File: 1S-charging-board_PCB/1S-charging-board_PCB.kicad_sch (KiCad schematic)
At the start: 4 parts, among them J1 Power Input, J2 Balance input, SW1 SW_Rotary_1x6_MP

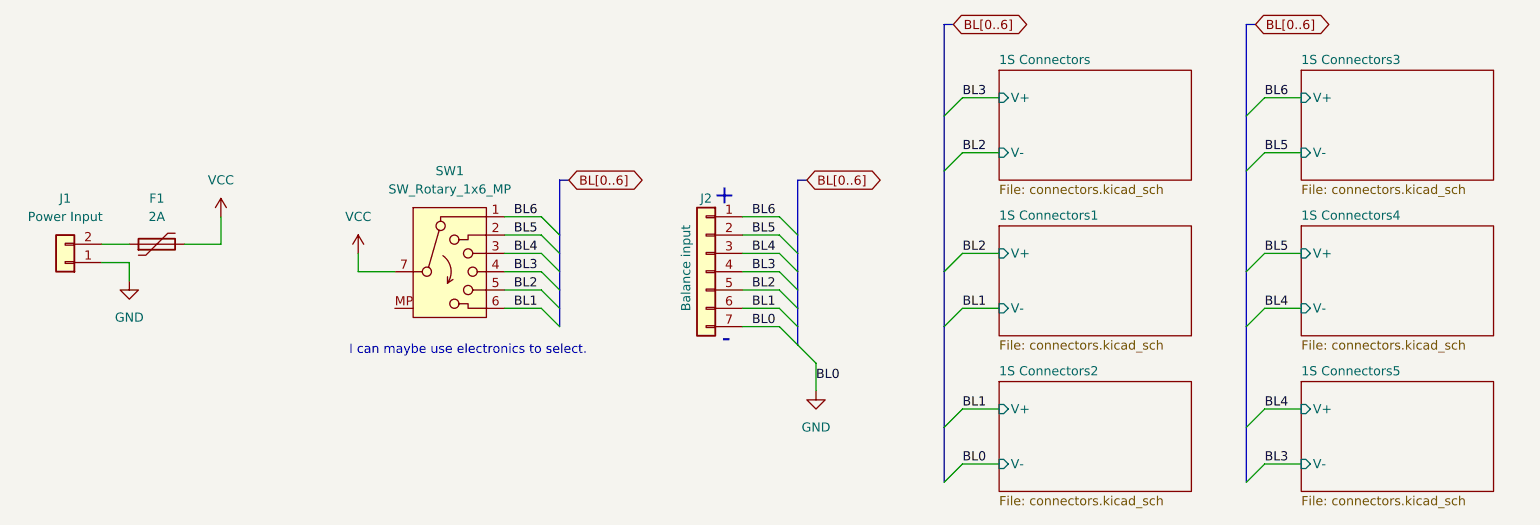
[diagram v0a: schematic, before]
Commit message: Finished the 1s charging board.
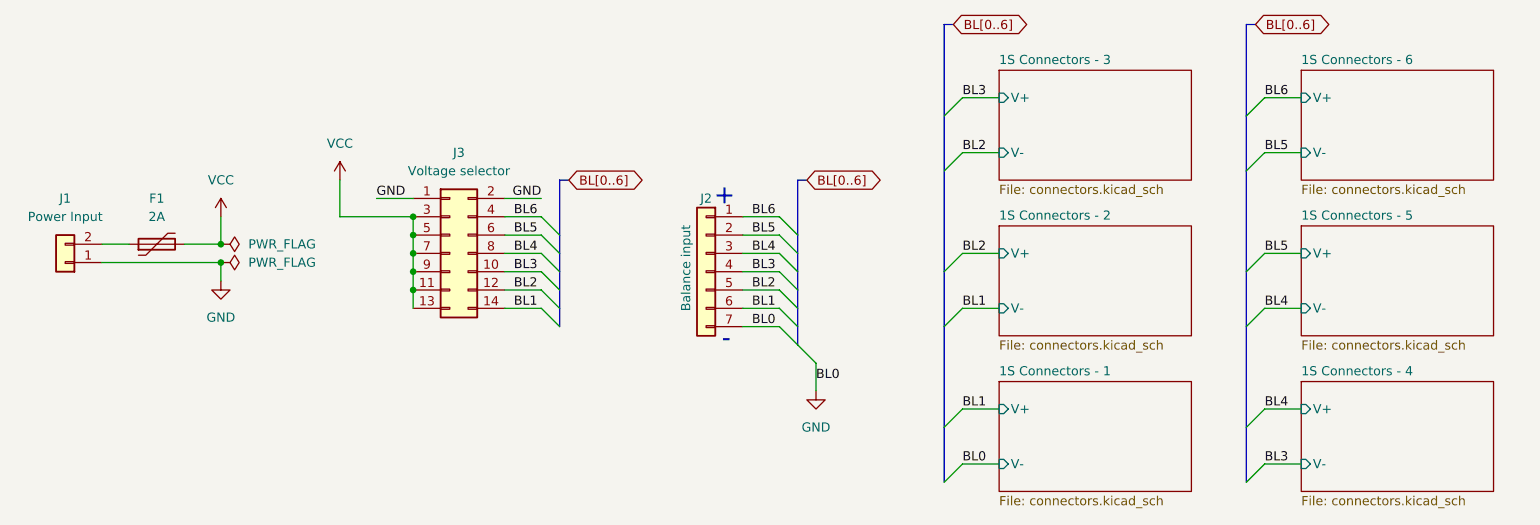
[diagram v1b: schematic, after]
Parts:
- removed SW1: SW_Rotary_1x6_MP, symbol Switch:SW_Rotary_1x6_MP
- added J3: Voltage selector, Connector_PinHeader_2.54mm:PinHeader_2x07_P2.54mm_Vertical, symbol Connector_Generic:Conn_02x07_Odd_Even
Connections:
- net BL1: now also J3.14 (Pin_14)
- net BL2: now also J3.12 (Pin_12)
- net BL3: now also J3.10 (Pin_10)
- net BL4: now also J3.8 (Pin_8)
- net BL5: now also J3.6 (Pin_6)
- net BL6: now also J3.4 (Pin_4)
- net GND: now also J3.1 (Pin_1), J3.2 (Pin_2)
- net VCC: now also J3.11 (Pin_11), J3.13 (Pin_13), J3.3 (Pin_3), J3.5 (Pin_5), J3.7 (Pin_7), J3.9 (Pin_9)
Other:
- sheet 1S Connectors renamed 1S Connectors - 1
- sheet 1S Connectors1 renamed 1S Connectors - 2
- sheet 1S Connectors2 renamed 1S Connectors - 3
- sheet 1S Connectors3 renamed 1S Connectors - 4
- sheet 1S Connectors4 renamed 1S Connectors - 5
- sheet 1S Connectors5 renamed 1S Connectors - 6
- note removed: "I can maybe use electronics to select."
